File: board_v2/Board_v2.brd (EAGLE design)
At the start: 135.1 x 89 mm, 42 parts, among them IC1 MAX7219, IC2 MAX7219, IC3 MAX7219, SW1 ROTARY SWITCH, SW2 ROTARY SWITCH

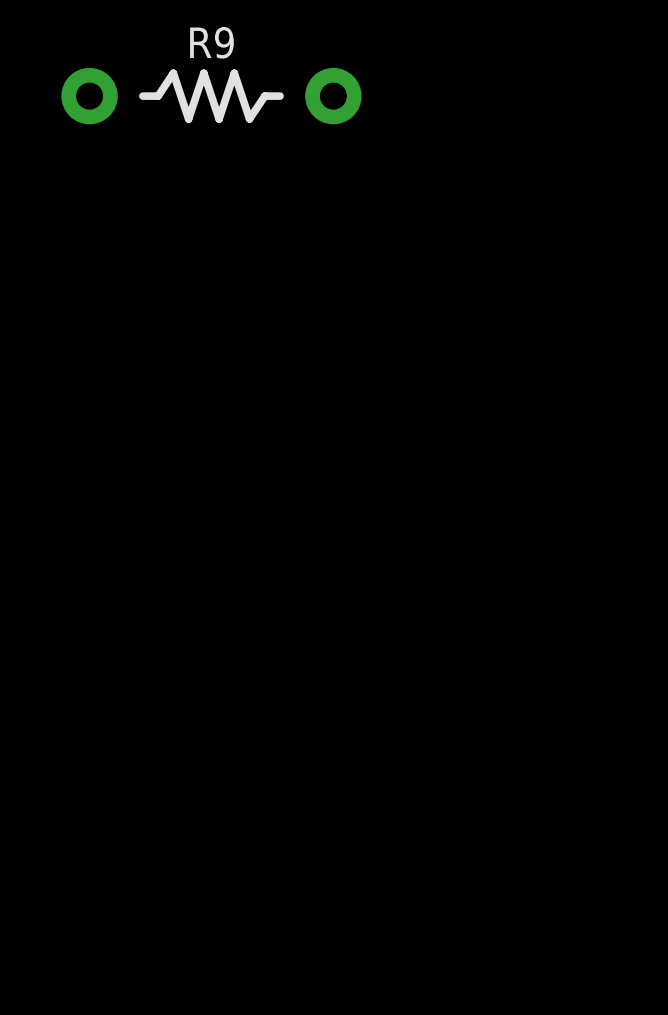
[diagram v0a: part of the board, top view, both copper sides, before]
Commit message: new annotations to boardv2 files
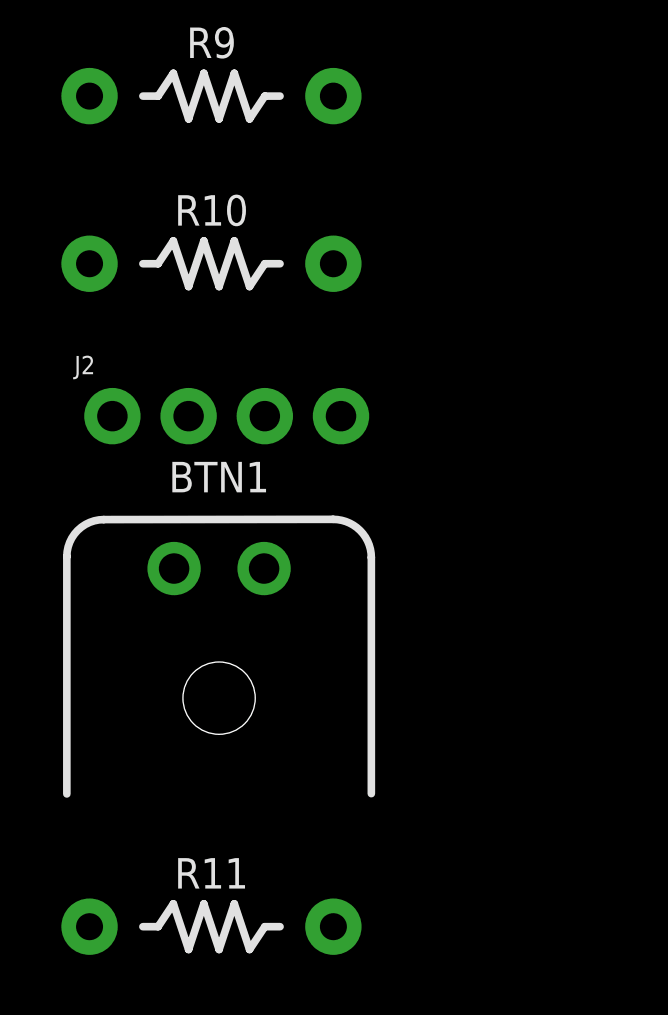
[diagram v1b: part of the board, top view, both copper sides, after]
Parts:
- added BTN1: CONN1, AES_lib:MICRO-FIT_43560_3MM
- added J2: (no value), SparkFun-Connectors:1X04_NO_SILK
- added R10, R11: 10k, AES_lib:AXIAL-0.3
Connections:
- net 3.3V: now also BTN1.P$1, J2.4
- net BTN: now also BTN1.P$2, R11.P$2
- net GND: now also J2.1, R10.P$1, R11.P$1
- net RESET: now also J2.2
- net STA: now also J2.3, R10.P$2
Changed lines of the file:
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@@
 <attribute name="VALUE" x="-43.18" y="-82.804" size="1.016" layer="27" font="vector" ratio="12" align="top-center"/>
+</element>
+<element name="J2" library="SparkFun-Connectors" library_urn="urn:adsk.eagle:library:513" package="1X04_NO_SILK" package3d_urn="urn:adsk.eagle:package:38094/1" value="" x="-46.482" y="-92.202" smashed="yes">
+<attribute name="NAME" x="-47.752" y="-90.805" size="0.6096" layer="25" font="vector" ratio="20"/>
+<attribute name="PROD_ID" value="CONN-09696" x="-46.482" y="-86.614" size="1.778" layer="27" display="off"/>
+<attribute name="VALUE" x="-47.752" y="-94.234" size="0.6096" layer="27" font="vector" ratio="20"/>
+</element>
+<element name="R10" library="AES_lib" library_urn="urn:adsk.eagle:library:7241092" package="AXIAL-0.3" package3d_urn="urn:adsk.eagle:package:7386443/1" value="10k" x="-43.18" y="-87.122" smashed="yes">
+<attribute name="NAME" x="-43.18" y="-85.852" size="1.016" layer="25" font="vector" ratio="12" align="bottom-center"/>
+<attribute name="VALUE" x="-43.18" y="-88.392" size="1.016" layer="27" font="vector" ratio="12" align="top-center"/>
+</element>
+<element name="BTN1" library="AES_lib" library_urn="urn:adsk.eagle:library:7241092" package="MICRO-FIT_43560_3MM" package3d_urn="urn:adsk.eagle:package:7386136/5" value="CONN1" x="-42.926" y="-97.282" smashed="yes">
+<attribute name="NAME" x="-42.926" y="-94.742" size="1.016" layer="25" font="vector" ratio="12" align="bottom-center"/>
+</element>
+<element name="R11" library="AES_lib" library_urn="urn:adsk.eagle:library:7241092" package="AXIAL-0.3" package3d_urn="urn:adsk.eagle:package:7386443/1" value="10k" x="-43.18" y="-109.22" smashed="yes">
+<attribute name="NAME" x="-43.18" y="-107.95" size="1.016" layer="25" font="vector" ratio="12" align="bottom-center"/>
+<attribute name="VALUE" x="-43.18" y="-110.49" size="1.016" layer="27" font="vector" ratio="12" align="top-center"/>
 </element>
 </elements>
@@
 <contactref element="R8" pad="P$1"/>
 <contactref element="R9" pad="P$1"/>
+<contactref element="J2" pad="1"/>
+<contactref element="R10" pad="P$1"/>
+<contactref element="R11" pad="P$1"/>
+<wire x1="-46.482" y1="-92.202" x2="-47.244" y2="-109.22" width="0" layer="19" extent="1-1"/>
+<wire x1="-47.244" y1="-87.122" x2="-46.482" y2="-92.202" width="0" layer="19" extent="1-1"/>
+<wire x1="-47.244" y1="-81.534" x2="-47.244" y2="-87.122" width="0" layer="19" extent="1-1"/>
 <wire x1="-47.244" y1="-75.946" x2="-47.244" y2="-81.534" width="0" layer="19" extent="1-1"/>
 <wire x1="-47.244" y1="-70.358" x2="-47.244" y2="-75.946" width="0" layer="19" extent="1-1"/>
@@
 <contactref element="R4" pad="P$2"/>
 <contactref element="SW2" pad="C1"/>
+<contactref element="J2" pad="4"/>
+<contactref element="BTN1" pad="P$1"/>
+<wire x1="-38.862" y1="-92.202" x2="-41.426" y2="-97.282" width="0" layer="19" extent="1-1"/>
+<wire x1="-34.29" y1="-60.198" x2="-38.862" y2="-92.202" width="0" layer="19" extent="1-1"/>
 <wire x1="5.126" y1="-16.406" x2="-34.29" y2="-60.198" width="0" layer="19" extent="1-1"/>
 <wire x1="-4.064" y1="2.5" x2="5.126" y2="-16.406" width="0" layer="19" extent="1-1"/>
@@
 <wire x1="74.6125" y1="-27.46375" x2="74.54" y2="-27.5" width="0.2286" layer="16"/>
 <via x="74.6125" y="-23.65375" extent="1-16" drill="0.3048"/>
+<contactref element="J2" pad="2"/>
+<wire x1="74.54" y1="-27.5" x2="-43.942" y2="-92.202" width="0" layer="19" extent="1-1"/>
 </signal>
 <signal name="BTN">
@@
 <wire x1="66.3575" y1="-36.67125" x2="66.492" y2="-36.703" width="0.2286" layer="16"/>
 <wire x1="52.22875" y1="2.06375" x2="52.2006" y2="2.1042" width="0.2286" layer="16"/>
+<contactref element="BTN1" pad="P$2"/>
+<contactref element="R11" pad="P$2"/>
+<wire x1="-44.426" y1="-97.282" x2="-39.116" y2="-109.22" width="0" layer="19" extent="1-1"/>
+<wire x1="58.89625" y1="-29.21" x2="-44.426" y2="-97.282" width="0" layer="19" extent="16-16"/>
 </signal>
 <signal name="STA">
@@
 <wire x1="76.99375" y1="-27.46375" x2="77.08" y2="-27.5" width="0.2286" layer="1"/>
 <via x="53.75275" y="-13.208" extent="1-16" drill="0.3048"/>
+<contactref element="J2" pad="3"/>
+<contactref element="R10" pad="P$2"/>
+<wire x1="-39.116" y1="-87.122" x2="-41.402" y2="-92.202" width="0" layer="19" extent="1-1"/>
+<wire x1="53.75275" y1="-13.208" x2="-39.116" y2="-87.122" width="0" layer="19" extent="16-16"/>
 </signal>
 </signals>

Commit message: boardv2 files annotated with new found errors
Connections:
- new net N$10: SEV8.7
- new net N$11: SEV10.7
- new net N$12: SEV5.7
- new net N$4: SEV4.7
- new net N$5: SEV3.7
- new net N$6: SEV2.7
- new net N$7: SEV1.7
- new net SOL: CONV.12, FEATHERM0.5
- net SEGDP1: no longer IC1.22
- net SEGDP2: no longer IC2.22
- net SEGDP3: no longer IC3.22
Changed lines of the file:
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@@
 <contactref element="BAR2" pad="10"/>
 <contactref element="BAR3" pad="10"/>
-<contactref element="IC1" pad="22"/>
 <wire x1="57.15" y1="32.7025" x2="57.4675" y2="32.385" width="0.2286" layer="16"/>
 <wire x1="57.15" y1="33.49625" x2="57.15" y2="32.7025" width="0.2286" layer="16"/>
@@
 <wire x1="37.30625" y1="37.62375" x2="53.0225" y2="37.62375" width="0.2286" layer="1"/>
 <wire x1="33.02" y1="41.91" x2="37.30625" y2="37.62375" width="0.2286" layer="1"/>
-<wire x1="57.4675" y1="32.385" x2="57.562" y2="32.38" width="0.2286" layer="16"/>
 <wire x1="33.02" y1="41.91" x2="33.0439" y2="41.9834" width="0.2286" layer="1"/>
 <wire x1="4.60375" y1="40.005" x2="2.69875" y2="41.91" width="0.2286" layer="16"/>
@@
 </signal>
 <signal name="SEGDP2">
-<contactref element="IC2" pad="22"/>
 <contactref element="BAR1" pad="10"/>
 <wire x1="43.4975" y1="16.1925" x2="43.4975" y2="17.30375" width="0.2286" layer="1"/>
@@
 <wire x1="-27.051" y1="40.005" x2="-18.034" y2="40.005" width="0.2286" layer="16"/>
 <wire x1="-27.78125" y1="41.91" x2="-27.46375" y2="41.5925" width="0.2286" layer="16"/>
-<wire x1="43.4975" y1="17.30375" x2="43.546" y2="17.348" width="0.2286" layer="1"/>
 <wire x1="-27.78125" y1="41.91" x2="-27.8706" y2="41.9832" width="0.2286" layer="16"/>
 <via x="34.6075" y="18.0975" extent="1-16" drill="0.3048"/>
@@
 </signal>
 <signal name="SEGDP3">
-<contactref element="IC3" pad="22"/>
 <contactref element="SEV7" pad="7"/>
 <contactref element="SEV9" pad="7"/>
@@
 <wire x1="-23.01875" y1="-40.3225" x2="-15.24" y2="-40.3225" width="0.2286" layer="1"/>
 <wire x1="-24.28875" y1="-39.0525" x2="-23.01875" y2="-40.3225" width="0.2286" layer="1"/>
-<wire x1="10.795" y1="-36.83" x2="10.872" y2="-36.836" width="0.2286" layer="1"/>
 <wire x1="-24.28875" y1="-39.0525" x2="-24.3245" y2="-39.033" width="0.2286" layer="1"/>
 <wire x1="-38.25875" y1="-40.3225" x2="-39.52875" y2="-39.0525" width="0.2286" layer="1"/>
@@
 <wire x1="10.95375" y1="-36.83" x2="16.35125" y2="-36.83" width="0.2286" layer="1"/>
 <wire x1="31.75" y1="12.065" x2="31.8556" y2="12.0734" width="0.2286" layer="16"/>
-<wire x1="10.95375" y1="-36.83" x2="10.872" y2="-36.836" width="0.2286" layer="1"/>
 <via x="22.70125" y="-37.94125" extent="1-16" drill="0.3048"/>
+<wire x1="10.95375" y1="-36.83" x2="10.795" y2="-36.83" width="0" layer="19" extent="1-1"/>
 </signal>
 <signal name="DIG42">
@@
 <wire x1="53.75275" y1="-13.208" x2="-39.116" y2="-87.122" width="0" layer="19" extent="16-16"/>
 </signal>
+<signal name="SOL">
+<contactref element="FEATHERM0" pad="5"/>
+<contactref element="CONV" pad="12"/>
+<wire x1="69.9806" y1="-18.2158" x2="71.6408" y2="8.3296" width="0" layer="19" extent="1-1"/>
+</signal>
+<signal name="N$4">
+<contactref element="SEV4" pad="7"/>
+</signal>
+<signal name="N$5">
+<contactref element="SEV3" pad="7"/>
+</signal>
+<signal name="N$6">
+<contactref element="SEV2" pad="7"/>
+</signal>
+<signal name="N$7">
+<contactref element="SEV1" pad="7"/>
+</signal>
+<signal name="N$10">
+<contactref element="SEV8" pad="7"/>
+</signal>
+<signal name="N$11">
+<contactref element="SEV10" pad="7"/>
+</signal>
+<signal name="N$12">
+<contactref element="SEV5" pad="7"/>
+</signal>
 </signals>
